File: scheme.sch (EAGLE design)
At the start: 49 parts, among them J1 22-05-7048-04, J2 22-05-7028-02

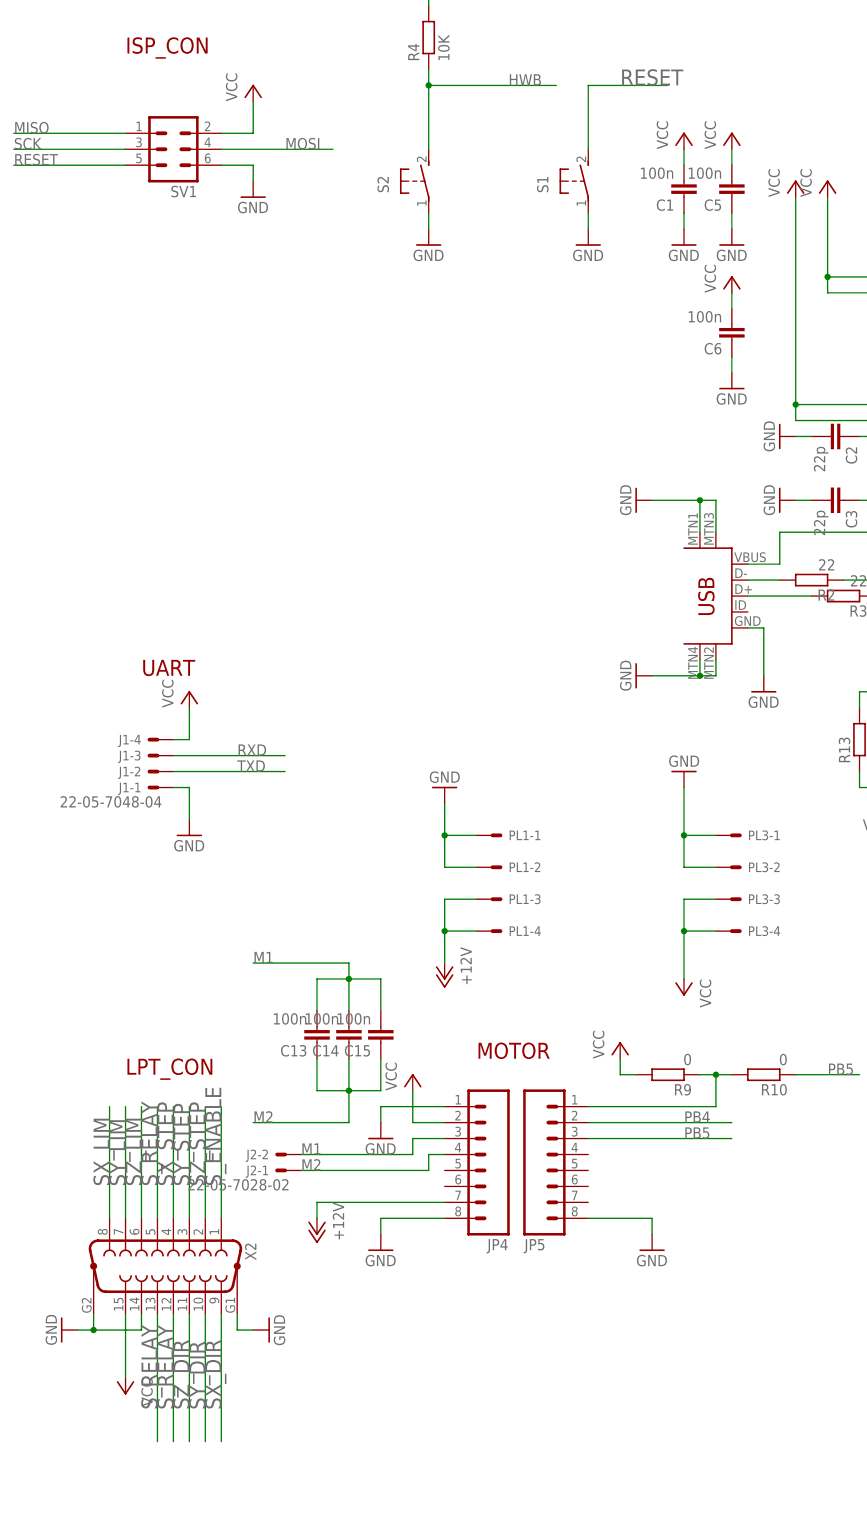
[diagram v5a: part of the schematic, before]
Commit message: Add D-SUB power jumper
Signed-off-by: Nikita 'webconn' Maslov <wkernelteam@gmail.com>
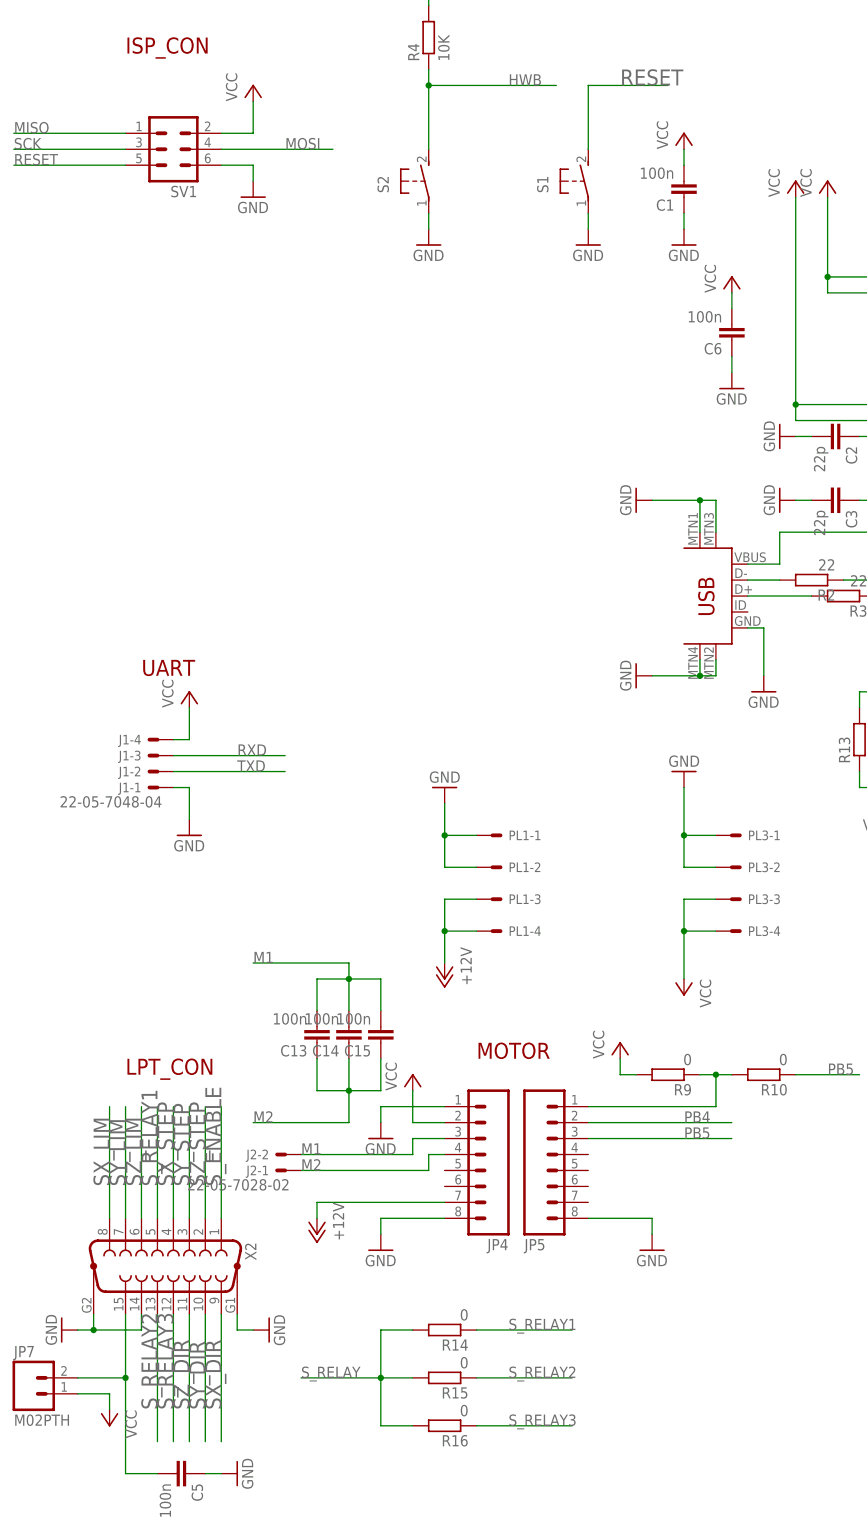
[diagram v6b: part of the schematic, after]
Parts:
- added JP7: M02PTH, SparkFun-Connectors:M02PTH
- added R14, R15, R16: 0, resistor:R-EU_R0805
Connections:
- new net N$16: C5.2, JP7.2, X2.15
- new net S_RELAY1: R14.1, X2.5
- new net S_RELAY2: R15.1, X2.13
- new net S_RELAY3: R16.1, X2.12
- net S_RELAY: now also R14.2, R15.2, R16.2; no longer X2.12, X2.13, X2.5
- net VCC: now also JP7.1; no longer C5.2, X2.15
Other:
- moved on the sheet: C5
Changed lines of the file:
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@@
 <part name="GND32" library="supply1" deviceset="GND" device=""/>
 <part name="C5" library="resistor" deviceset="C-EU" device="C0805" value="100n"/>
-<part name="P+21" library="supply1" deviceset="VCC" device=""/>
 <part name="GND33" library="supply1" deviceset="GND" device=""/>
 <part name="C6" library="resistor" deviceset="C-EU" device="C0805" value="100n"/>
@@
 <part name="P+26" library="supply1" deviceset="VCC" device=""/>
 <part name="R13" library="rcl" deviceset="R-EU_" device="R1206" value="0"/>
+<part name="R14" library="resistor" deviceset="R-EU_" device="R0805" value="0"/>
+<part name="R15" library="resistor" deviceset="R-EU_" device="R0805" value="0"/>
+<part name="R16" library="resistor" deviceset="R-EU_" device="R0805" value="0"/>
+<part name="JP7" library="SparkFun-Connectors" deviceset="M02" device="PTH"/>
 </parts>
 <sheets>
@@
 <instance part="GND12" gate="1" x="60.96" y="30.48" rot="R90"/>
 <instance part="GND13" gate="1" x="27.94" y="30.48" rot="R270"/>
-<instance part="P+8" gate="VCC" x="38.1" y="20.32" rot="R180"/>
+<instance part="P+8" gate="VCC" x="35.56" y="15.24" rot="R180"/>
 <instance part="R5" gate="G$1" x="185.42" y="63.5" rot="R90"/>
 <instance part="P+9" gate="VCC" x="195.58" y="76.2"/>
@@
 <instance part="GND31" gate="1" x="248.92" y="236.22"/>
 <instance part="GND32" gate="1" x="264.16" y="236.22"/>
-<instance part="C5" gate="G$1" x="134.62" y="210.82" rot="R180"/>
-<instance part="P+21" gate="VCC" x="134.62" y="220.98"/>
-<instance part="GND33" gate="1" x="134.62" y="203.2"/>
+<instance part="C5" gate="G$1" x="48.26" y="7.62" rot="R270"/>
+<instance part="GND33" gate="1" x="55.88" y="7.62" rot="R90"/>
 <instance part="C6" gate="G$1" x="134.62" y="187.96" rot="R180"/>
 <instance part="P+22" gate="VCC" x="134.62" y="198.12"/>
@@
 <instance part="P+26" gate="VCC" x="157.48" y="114.3" rot="R90"/>
 <instance part="R13" gate="G$1" x="154.94" y="124.46" rot="R90"/>
+<instance part="R14" gate="G$1" x="88.9" y="30.48" rot="R180"/>
+<instance part="R15" gate="G$1" x="88.9" y="22.86" rot="R180"/>
+<instance part="R16" gate="G$1" x="88.9" y="15.24" rot="R180"/>
+<instance part="JP7" gate="G$1" x="22.86" y="20.32"/>
 </instances>
 <busses>
@@
 <pinref part="C5" gate="G$1" pin="1"/>
 <pinref part="GND33" gate="1" pin="GND"/>
-<wire x1="134.62" y1="208.28" x2="134.62" y2="205.74" width="0.1524" layer="91"/>
+<wire x1="50.8" y1="7.62" x2="53.34" y2="7.62" width="0.1524" layer="91"/>
 </segment>
 <segment>
@@
 </segment>
 <segment>
-<pinref part="X2" gate="G$1" pin="15"/>
-<wire x1="38.1" y1="33.02" x2="38.1" y2="22.86" width="0.1524" layer="91"/>
-<pinref part="P+8" gate="VCC" pin="VCC"/>
-</segment>
-<segment>
 <pinref part="P+9" gate="VCC" pin="VCC"/>
 <wire x1="185.42" y1="71.12" x2="195.58" y2="71.12" width="0.1524" layer="91"/>
@@
 <pinref part="R4" gate="G$1" pin="2"/>
 <wire x1="86.36" y1="243.84" x2="86.36" y2="241.3" width="0.1524" layer="91"/>
-</segment>
-<segment>
-<pinref part="P+21" gate="VCC" pin="VCC"/>
-<pinref part="C5" gate="G$1" pin="2"/>
-<wire x1="134.62" y1="218.44" x2="134.62" y2="215.9" width="0.1524" layer="91"/>
 </segment>
 <segment>
@@
 <pinref part="JP6" gate="G$1" pin="2"/>
 <wire x1="160.02" y1="114.3" x2="167.64" y2="114.3" width="0.1524" layer="91"/>
+</segment>
+<segment>
+<pinref part="JP7" gate="G$1" pin="1"/>
+<pinref part="P+8" gate="VCC" pin="VCC"/>
+<wire x1="30.48" y1="20.32" x2="35.56" y2="20.32" width="0.1524" layer="91"/>
+<wire x1="35.56" y1="20.32" x2="35.56" y2="17.78" width="0.1524" layer="91"/>
 </segment>
 </net>
@@
 <net name="S_RELAY" class="0">
 <segment>
+<pinref part="U$1" gate="G$1" pin="(ADC0)PF0"/>
+<wire x1="236.22" y1="137.16" x2="259.08" y2="137.16" width="0.1524" layer="91"/>
+<label x="251.46" y="137.16" size="1.778" layer="95"/>
+</segment>
+<segment>
+<pinref part="R14" gate="G$1" pin="2"/>
+<wire x1="83.82" y1="30.48" x2="78.74" y2="30.48" width="0.1524" layer="91"/>
+<wire x1="78.74" y1="30.48" x2="78.74" y2="22.86" width="0.1524" layer="91"/>
+<pinref part="R16" gate="G$1" pin="2"/>
+<wire x1="78.74" y1="22.86" x2="78.74" y2="15.24" width="0.1524" layer="91"/>
+<wire x1="78.74" y1="15.24" x2="83.82" y2="15.24" width="0.1524" layer="91"/>
+<pinref part="R15" gate="G$1" pin="2"/>
+<wire x1="83.82" y1="22.86" x2="78.74" y2="22.86" width="0.1524" layer="91"/>
+<junction x="78.74" y="22.86"/>
+<wire x1="78.74" y1="22.86" x2="66.04" y2="22.86" width="0.1524" layer="91"/>
+<label x="66.04" y="22.86" size="1.778" layer="95"/>
+</segment>
+</net>
+<net name="S_RELAY1" class="0">
+<segment>
 <pinref part="X2" gate="G$1" pin="5"/>
 <wire x1="43.18" y1="48.26" x2="43.18" y2="66.04" width="0.1524" layer="91"/>
@@
 </segment>
 <segment>
-<pinref part="U$1" gate="G$1" pin="(ADC0)PF0"/>
-<wire x1="236.22" y1="137.16" x2="259.08" y2="137.16" width="0.1524" layer="91"/>
-<label x="251.46" y="137.16" size="1.778" layer="95"/>
-</segment>
+<pinref part="R14" gate="G$1" pin="1"/>
+<wire x1="93.98" y1="30.48" x2="109.22" y2="30.48" width="0.1524" layer="91"/>
+<label x="99.06" y="30.48" size="1.778" layer="95"/>
+</segment>
+</net>
+<net name="S_RELAY2" class="0">
 <segment>
 <pinref part="X2" gate="G$1" pin="13"/>
@@
 </segment>
 <segment>
+<pinref part="R15" gate="G$1" pin="1"/>
+<wire x1="93.98" y1="22.86" x2="109.22" y2="22.86" width="0.1524" layer="91"/>
+<label x="99.06" y="22.86" size="1.778" layer="95"/>
+</segment>
+</net>
+<net name="S_RELAY3" class="0">
+<segment>
 <pinref part="X2" gate="G$1" pin="12"/>
 <wire x1="45.72" y1="33.02" x2="45.72" y2="12.7" width="0.1524" layer="91"/>
 <label x="45.72" y="17.78" size="2.54" layer="95" rot="R90"/>
 </segment>
-</net>
+<segment>
+<pinref part="R16" gate="G$1" pin="1"/>
+<wire x1="93.98" y1="15.24" x2="109.22" y2="15.24" width="0.1524" layer="91"/>
+<label x="99.06" y="15.24" size="1.778" layer="95"/>
+</segment>
+</net>
+<net name="N$16" class="0">
+<segment>
+<pinref part="X2" gate="G$1" pin="15"/>
+<wire x1="38.1" y1="33.02" x2="38.1" y2="22.86" width="0.1524" layer="91"/>
+<pinref part="JP7" gate="G$1" pin="2"/>
+<wire x1="38.1" y1="22.86" x2="30.48" y2="22.86" width="0.1524" layer="91"/>
+<wire x1="38.1" y1="22.86" x2="38.1" y2="7.62" width="0.1524" layer="91"/>
+<junction x="38.1" y="22.86"/>
+<pinref part="C5" gate="G$1" pin="2"/>
+<wire x1="38.1" y1="7.62" x2="43.18" y2="7.62" width="0.1524" layer="91"/>
+</segment>
+</net>
